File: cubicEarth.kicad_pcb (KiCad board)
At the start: 2 copper layers, 32 x 35 mm, 33 parts, among them J1 TYPE-C-31-M-12, J2 LCD, Q1 BC847BVC-7, SW1 TS24ZJ, U1 CP2102N-A02-GQFN24R, U2 AW9364DNR, U3 LP2992AIM5X-3.3, U4 ESP32-PICO-V3-02

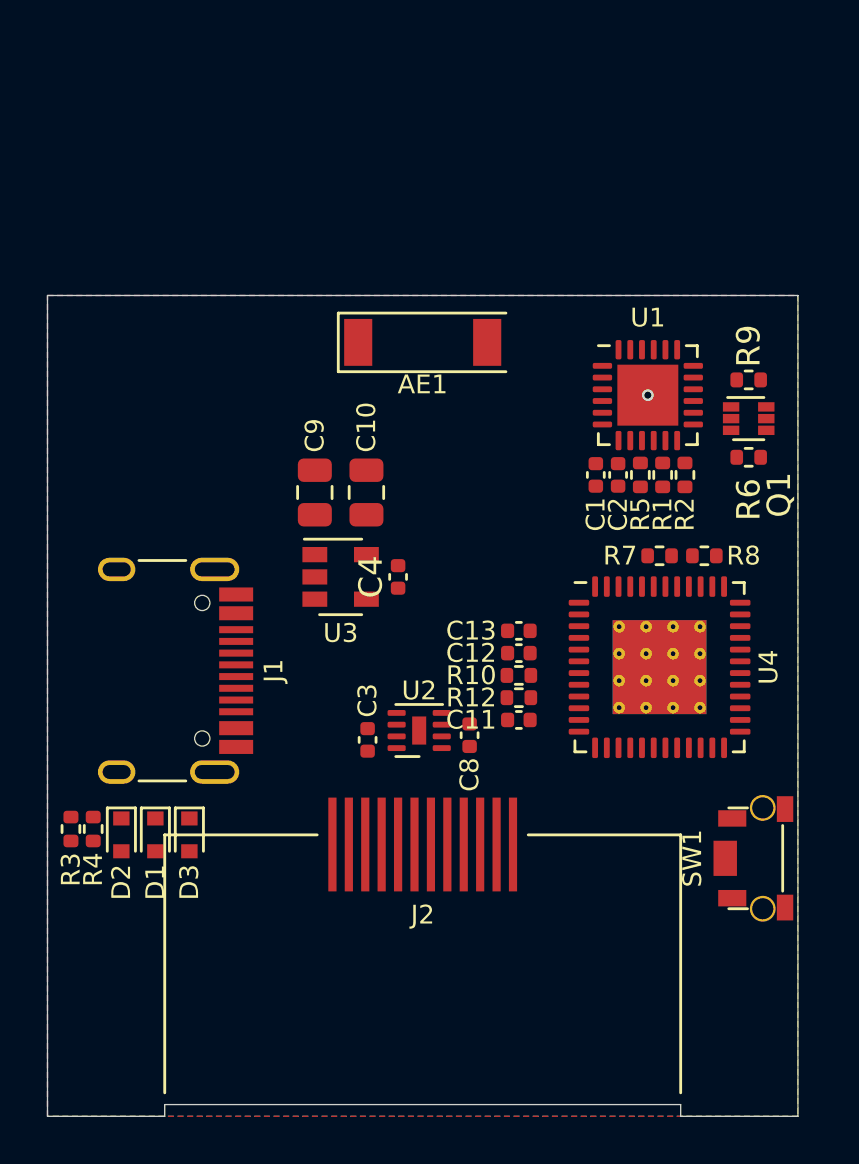
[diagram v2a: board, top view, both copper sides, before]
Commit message: PCB layout almost done
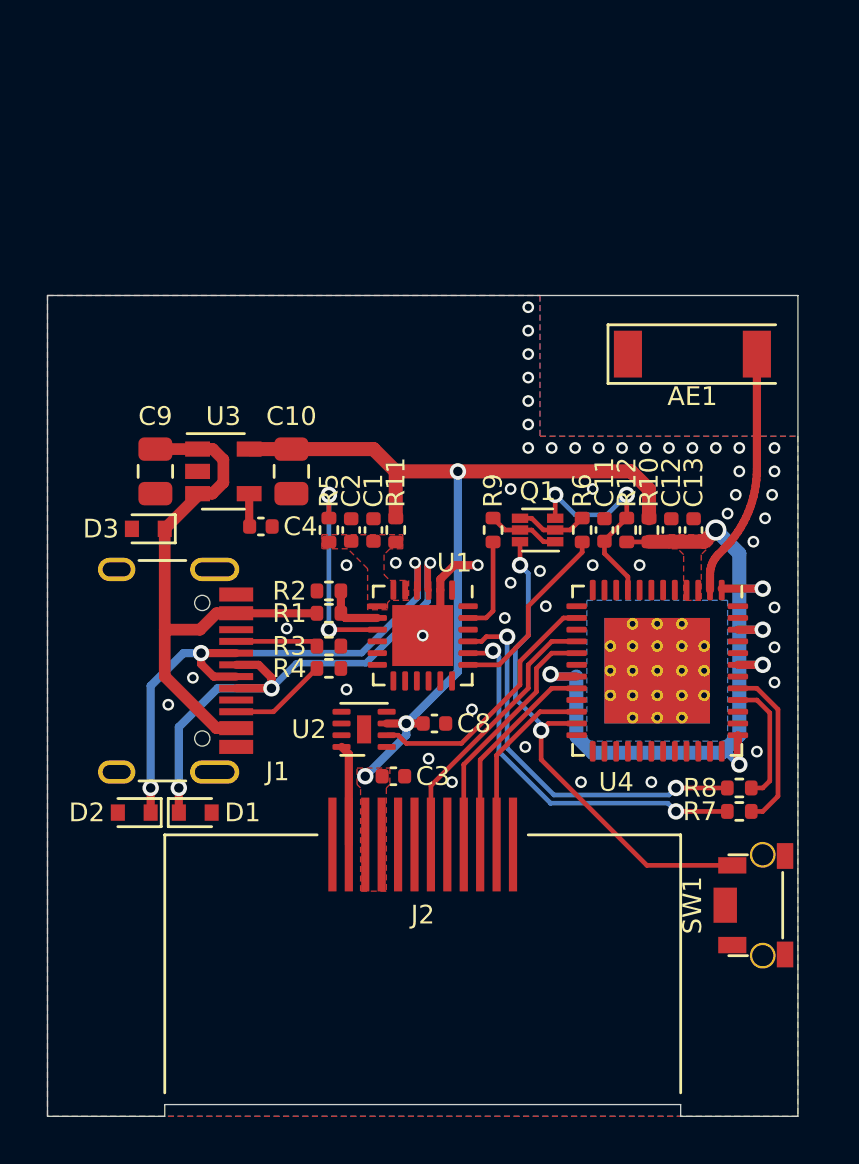
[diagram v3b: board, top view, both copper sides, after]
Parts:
- added R11: 0, Resistor_SMD:R_0402_1005Metric, F.Cu at (98.8, 94.0)
- J2: value LCD -> ZJY154T-PG04
- U4: footprint JLC-SMT:QFN-48-1EP_7x7mm_P0.5mm_EP4x4mm_ThermalVias -> JLC-SMT:ESP32-PICO_QFN-48_7x7mm_P0.5mm_EP4.5x4.5mm_ThermalVias
- moved R2 16.0 mm to (96.0, 96.6), turned to 180 degrees
- moved R1 15.4 mm to (96.0, 97.5), turned to 180 degrees
- moved U1 14.0 mm to (100.0, 98.5), turned to 270 degrees
- moved R5 13.5 mm to (96.0, 94.0)
- moved R3 13.5 mm to (96.0, 99.0), turned to 180 degrees
- moved D3 13.2 mm to (88.3, 94.0), turned to 180 degrees
- moved R9 12.6 mm to (103.0, 94.0), turned to 90 degrees
- moved R4 12.2 mm to (96.0, 99.9), turned to 180 degrees
- moved C2 11.6 mm to (97.0, 94.0), turned to 90 degrees
- moved AE1 11.5 mm to (111.5, 86.5)
- moved R7 11.4 mm to (113.5, 106.0)
- moved Q1 10.2 mm to (104.9, 94.0), turned to 180 degrees
- moved R8 10.0 mm to (113.5, 105.0), turned to 180 degrees
- moved C1 9.77 mm to (97.9, 94.0), turned to 90 degrees
- moved C11 8.88 mm to (107.8, 94.0), turned to 90 degrees
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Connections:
- C1 pad 1: +3V3 -> Net-(C1-Pad1)
- C2 pad 1: +3V3 -> Net-(C1-Pad1)
- J2 pad 8: /LCD_CS -> GND
- R5 pad 2: +3V3 -> Net-(C1-Pad1)
- U1 pad 5: +3V3 -> Net-(C1-Pad1)
- U1 pad 6: +3V3 -> Net-(C1-Pad1)
- U1 pad 7: +3V3 -> Net-(C1-Pad1)
- U4 pad 15: /LCD_RES -> (no net)
- U4 pad 21: /LCD_CS -> (no net)
- U4 pad 22: (no net) -> /LCD_RES
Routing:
- net +3V3: track 0.00 -> 37.1 mm, vias 0 -> 3
- net /ESP_VDD: track 0.00 -> 34.7 mm, vias 0 -> 6
- net /D-: track 0.00 -> 24.8 mm, vias 0 -> 3
- net +5V: track 0.00 -> 24.4 mm
- net /D+: track 0.00 -> 23.1 mm, vias 0 -> 3
- net /BOOT: track 0.00 -> 21.8 mm, vias 0 -> 2
- net /USB_TX: track 0.00 -> 16.8 mm, vias 0 -> 2
- net /USB_RX: track 0.00 -> 16.3 mm, vias 0 -> 2
- net /LCD_DC: track 0.00 -> 11.9 mm
- net /BLK: track 0.00 -> 11.0 mm
- net /LCD_SCL: track 0.00 -> 10.8 mm
- net Net-(AE1-Pad1): track 0.00 -> 10.6 mm
- net /EN: track 0.00 -> 9.62 mm, vias 0 -> 2
- net /LCD_SDA: track 0.00 -> 8.98 mm
- net Net-(R5-Pad1): track 0.00 -> 8.80 mm, vias 0 -> 2
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- added copper zone on F.Cu, net +3V3
- added copper zone on F.Cu, net /ESP_VDD
- added copper zone on F.Cu, net Net-(C1-Pad1)

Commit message: Looks better
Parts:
- moved D3 12.9 mm to (92.9, 106.0)
- moved C4 1.96 mm to (95.0, 94.0), turned to 270 degrees
- moved C10 1.38 mm to (93.4, 92.5)
- moved C9 1.38 mm to (87.6, 92.5)
- moved U3 1.38 mm to (90.5, 92.4)
- moved R4 0.25 mm to (96.0, 100.2)
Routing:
- net +5V: track 24.4 -> 27.2 mm
- net Net-(C4-Pad1): track 1.40 -> 4.03 mm
- net +3V3: track 37.1 -> 37.7 mm
- net GND: vias 50 -> 55

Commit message: Looks even better
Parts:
- moved C10 0.40 mm to (93.4, 92.8)
- moved C9 0.40 mm to (87.6, 92.8)
- moved U3 0.40 mm to (90.5, 92.8)
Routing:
- net Net-(C4-Pad1): track 4.03 -> 5.56 mm, vias 0 -> 2
- net GND: vias 55 -> 61
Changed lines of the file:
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@@
     (thickness 1.2)
     (drawings 23)
-    (tracks 301)
+    (tracks 311)
     (zones 0)
     (modules 34)
@@
   )
   (module Package_TO_SOT_SMD:SOT-23-5 (layer F.Cu)
-    (at 90.5 92.449999)
+    (at 90.5 92.849999)
     (descr "5-pin SOT23 package")
     (tags SOT-23-5)
@@
   )
   (module Capacitor_SMD:C_0805_2012Metric (layer F.Cu)
-    (at 93.4 92.45 270)
+    (at 93.4 92.85 270)
     (descr "Capacitor SMD 0805 (2012 Metric), square (rectangular) end terminal, IPC_7351 nominal, (Body size source: IPC-SM-782 page 76, https://www.pcb-3d.com/wordpress/wp-content/uploads/ipc-sm-782a_amendment_1_and_2.pdf, https://docs.google.com/spreadsheets/d/1BsfQQcO9C6DZCsRaXUlFlo91Tg2WpOkGARC1WS5S8t0/edit?usp=sharing), generated with kicad-footprint-generator")
     (tags capacitor)
@@
   )
   (module Capacitor_SMD:C_0805_2012Metric (layer F.Cu)
-    (at 87.6 92.45 270)
+    (at 87.6 92.85 270)
     (descr "Capacitor SMD 0805 (2012 Metric), square (rectangular) end terminal, IPC_7351 nominal, (Body size source: IPC-SM-782 page 76, https://www.pcb-3d.com/wordpress/wp-content/uploads/ipc-sm-782a_amendment_1_and_2.pdf, https://docs.google.com/spreadsheets/d/1BsfQQcO9C6DZCsRaXUlFlo91Tg2WpOkGARC1WS5S8t0/edit?usp=sharing), generated with kicad-footprint-generator")
     (tags capacitor)
@@
   (via (at 98.8 95.5) (size 0.5) (drill 0.3) (layers F.Cu B.Cu) (net 1))
   (via (at 94.5 100.8) (size 0.5) (drill 0.3) (layers F.Cu B.Cu) (net 1))
-  (via (at 91.6 92.45) (size 0.5) (drill 0.3) (layers F.Cu B.Cu) (net 1))
-  (via (at 94.8 92.45) (size 0.5) (drill 0.3) (layers F.Cu B.Cu) (net 1))
   (via (at 97.85 92.45) (size 0.5) (drill 0.3) (layers F.Cu B.Cu) (net 1))
   (via (at 100.5 92.45) (size 0.5) (drill 0.3) (layers F.Cu B.Cu) (net 1))
+  (via (at 94 95.5) (size 0.5) (drill 0.3) (layers F.Cu B.Cu) (net 1))
+  (via (at 95 103.5) (size 0.5) (drill 0.3) (layers F.Cu B.Cu) (net 1))
+  (via (at 95 106) (size 0.5) (drill 0.3) (layers F.Cu B.Cu) (net 1))
+  (via (at 89 104) (size 0.5) (drill 0.3) (layers F.Cu B.Cu) (net 1))
+  (via (at 87.5 108.5) (size 0.5) (drill 0.3) (layers F.Cu B.Cu) (net 1))
+  (via (at 105 106.5) (size 0.5) (drill 0.3) (layers F.Cu B.Cu) (net 1))
+  (via (at 109.5 106.5) (size 0.5) (drill 0.3) (layers F.Cu B.Cu) (net 1))
+  (via (at 100.75 94.2) (size 0.5) (drill 0.3) (layers F.Cu B.Cu) (net 1))
   (via (at 93.55 100.75) (size 0.7) (drill 0.4) (layers F.Cu B.Cu) (net 2))
   (segment (start 94.62 99.68) (end 97.574056 99.68) (width 0.28) (layer B.Cu) (net 2))
@@
   (segment (start 90.505 98.25) (end 89.4 98.25) (width 0.5) (layer F.Cu) (net 4))
   (segment (start 89.4 98.25) (end 89.4 100.645) (width 0.5) (layer F.Cu) (net 4))
-  (segment (start 89.4 93.399999) (end 89.4 98.25) (width 0.5) (layer F.Cu) (net 4))
-  (segment (start 90.330001 93.095) (end 90.025001 93.4) (width 0.5) (layer F.Cu) (net 4))
-  (segment (start 90.330001 91.804998) (end 90.330001 93.095) (width 0.5) (layer F.Cu) (net 4))
-  (segment (start 90.025003 91.5) (end 90.330001 91.804998) (width 0.5) (layer F.Cu) (net 4))
-  (segment (start 87.6 91.5) (end 90.025003 91.5) (width 0.5) (layer F.Cu) (net 4))
-  (segment (start 90.025001 93.4) (end 89.4 93.4) (width 0.5) (layer F.Cu) (net 4))
+  (segment (start 90.330001 93.495) (end 90.025001 93.8) (width 0.5) (layer F.Cu) (net 4))
+  (segment (start 90.330001 92.204998) (end 90.330001 93.495) (width 0.5) (layer F.Cu) (net 4))
+  (segment (start 90.025003 91.9) (end 90.330001 92.204998) (width 0.5) (layer F.Cu) (net 4))
+  (segment (start 87.6 91.9) (end 90.025003 91.9) (width 0.5) (layer F.Cu) (net 4))
+  (segment (start 90.025001 93.8) (end 89.4 93.8) (width 0.5) (layer F.Cu) (net 4))
+  (segment (start 89.4 93.799999) (end 89.4 98.25) (width 0.5) (layer F.Cu) (net 4))
   (segment (start 109.65 92.265998) (end 109.65 93.5) (width 0.6) (layer F.Cu) (net 5))
   (segment (start 98.85 91.5) (end 98.85 93.45) (width 0.6) (layer F.Cu) (net 5))
@@
   (segment (start 99.3 102.75) (end 97.55 104.5) (width 0.35) (layer B.Cu) (net 5))
   (segment (start 99.3 102.25) (end 99.3 102.75) (width 0.35) (layer B.Cu) (net 5))
-  (segment (start 92.730001 91.5) (end 98.85 91.5) (width 0.6) (layer F.Cu) (net 5))
-  (segment (start 91.6 91.499999) (end 92.730001 91.5) (width 0.6) (layer F.Cu) (net 5))
+  (segment (start 98.85 91.5) (end 93.8 91.5) (width 0.6) (layer F.Cu) (net 5))
+  (segment (start 93.8 91.5) (end 93.4 91.9) (width 0.6) (layer F.Cu) (net 5))
+  (segment (start 93.4 91.9) (end 91.6 91.9) (width 0.6) (layer F.Cu) (net 5))
   (segment (start 106 97.75) (end 106.5625 97.75) (width 0.2) (layer F.Cu) (net 6))
   (segment (start 104.14998 99.60002) (end 106 97.75) (width 0.2) (layer F.Cu) (net 6))
@@
   (segment (start 102.7 97.75) (end 103 97.45) (width 0.2) (layer F.Cu) (net 27))
   (segment (start 103 94.51) (end 103 97.45) (width 0.2) (layer F.Cu) (net 27))
-  (segment (start 92.350011 94.15001) (end 94.39999 94.15001) (width 0.2) (layer F.Cu) (net 28))
-  (segment (start 91.6 93.399999) (end 92.350011 94.15001) (width 0.2) (layer F.Cu) (net 28))
-  (segment (start 94.39999 94.15001) (end 95.05 93.5) (width 0.2) (layer F.Cu) (net 28))
+  (via (at 91.6 92.85) (size 0.7) (drill 0.4) (layers F.Cu B.Cu) (net 28))
+  (segment (start 91.6 93.799999) (end 91.6 92.85) (width 0.2) (layer F.Cu) (net 28))
+  (via (at 95.05 92.5) (size 0.7) (drill 0.4) (layers F.Cu B.Cu) (net 28))
+  (segment (start 94.7 92.85) (end 95.05 92.5) (width 0.2) (layer B.Cu) (net 28))
+  (segment (start 91.6 92.85) (end 94.7 92.85) (width 0.2) (layer B.Cu) (net 28))
+  (segment (start 95.05 93.52) (end 95.05 92.5) (width 0.2) (layer F.Cu) (net 28))
   (zone (net 1) (net_name GND) (layer F.Cu) (hatch edge 0.508)
     (connect_pads (clearance 0.15))
